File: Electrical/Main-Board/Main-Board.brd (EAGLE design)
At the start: 160 x 100 mm, 10 parts, among them IC1 ATMEGA16A-PU, IC2 ATMEGA16A-PU, J1 FTSH-105-01-L-DV-K-A-P-TR

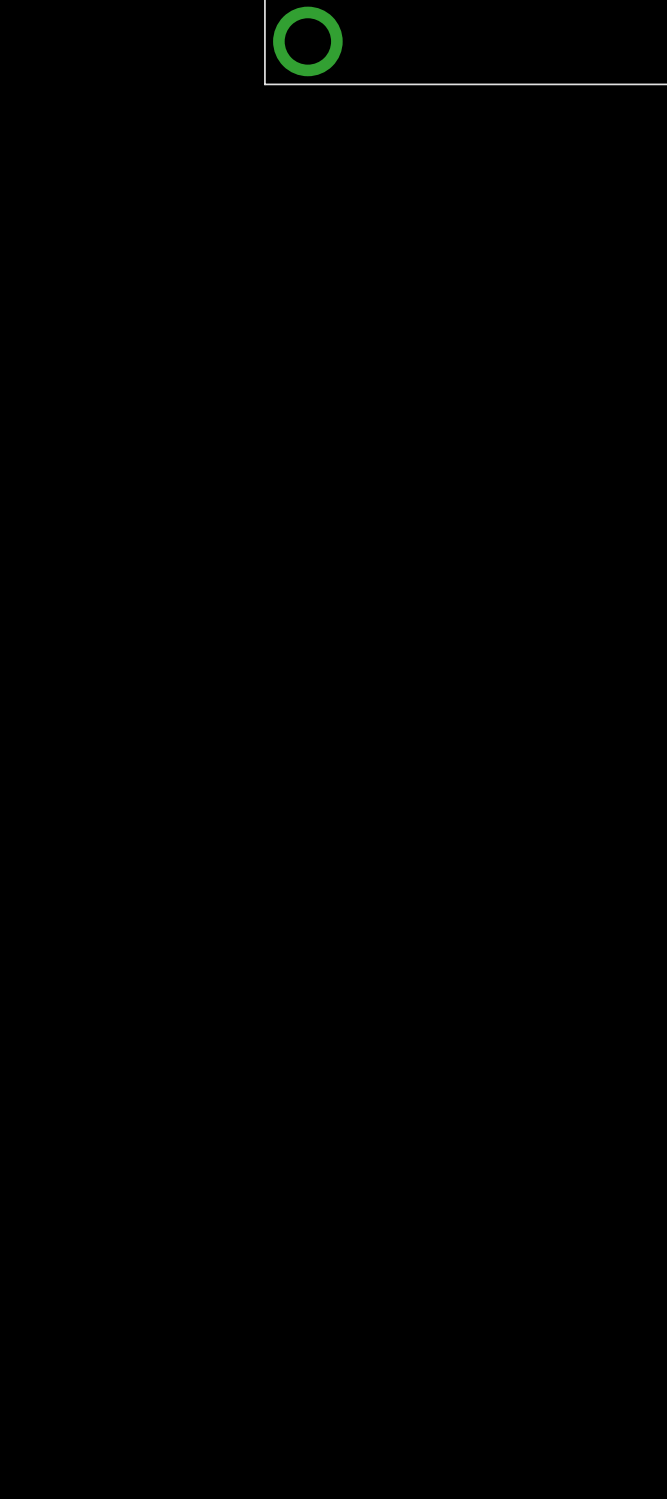
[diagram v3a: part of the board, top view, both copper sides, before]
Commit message: Added motor things to schematic
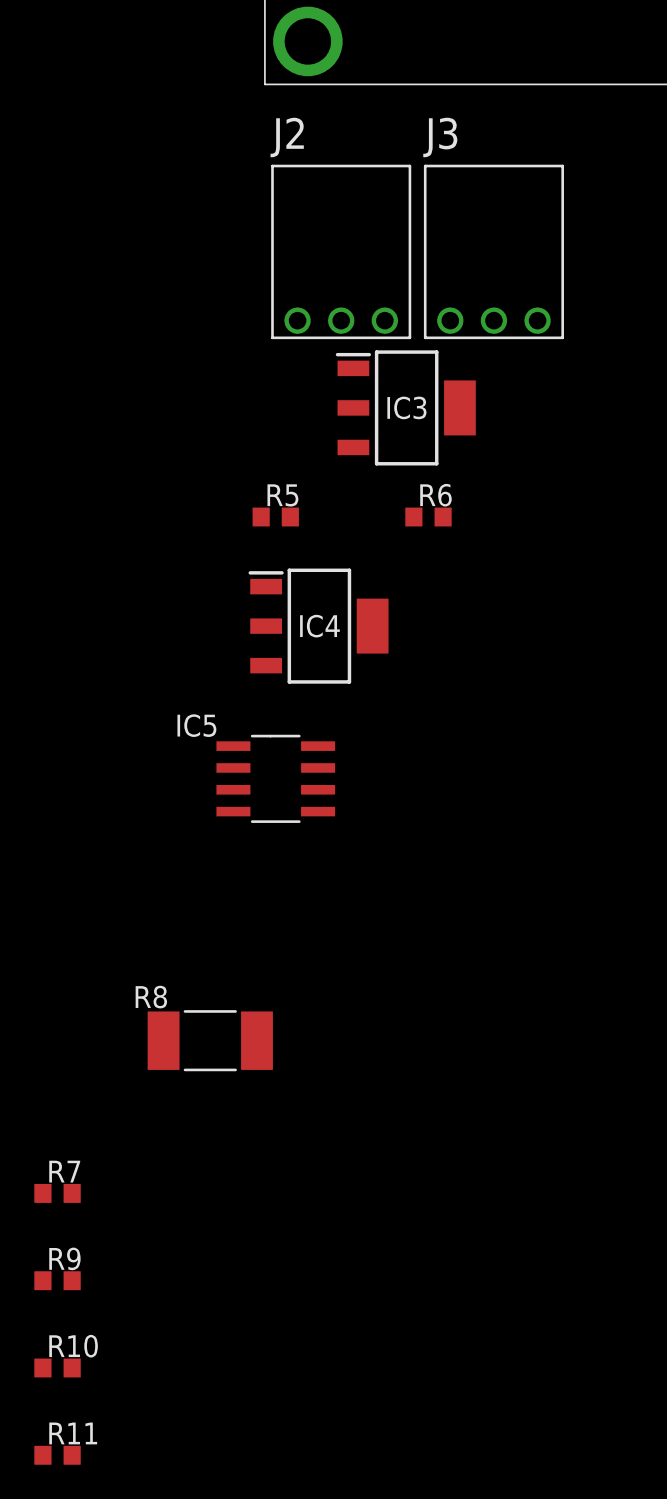
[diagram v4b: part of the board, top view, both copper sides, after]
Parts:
- added IC3: AZ1117CH-ADJTRG1, SamacSys_Parts:SOT230P700X170-4N
- added IC4: AZ1117CH-5.0TRG1DITR-ND, SamacSys_Parts:SOT230P700X180-4N
- added IC5: LM2904DRG3, SamacSys_Parts:SOIC127P600X175-8N
- added J2, J3: 0022288033, 0022288033:0022288033
- added R10, R11: 10K/5%, rcl:R0603
- added R5: 200R/5%, rcl:R0603
- added R6: 866R/5%, rcl:R0603
- added R7, R9: 100R/5%, rcl:R0603
- added R8: ERJ-L1WKF10CU, SamacSys_Parts:RESC6332X120N
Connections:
- new net +12V: IC3.3, IC4.3
- new net +7.5V: J2.P$2, J3.P$2, R8.2, R9.1
- new net DABDA: IC3.2, IC3.4, R5.2, R7.1, R8.1
- new net MOTOR_OVER-CURRENT: IC2.3, IC5.1, R10.2
- new net N$1: IC5.3, R11.2, R7.2
- new net N$5: IC5.2, R10.1, R9.2
- new net SERVO-LOWER: IC2.19, J3.P$3
- new net SERVO-UPPER: IC2.18, J2.P$3
- new net W3R355: IC3.1, R5.1, R6.2
- net +5V/1: now also IC4.2, IC4.4, IC5.8
- net GND: now also IC4.1, IC5.4, J2.P$1, J3.P$1, R11.1, R6.1

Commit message: Did some layout
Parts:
- added J4: PJ-031DH, SamacSys_Parts:PJ031DH
- moved IC5 195.2 mm to (91.0, -16.0)
- moved R7 195.1 mm to (78.0, -40.0)
- moved R6 195.1 mm to (100.0, -1.00)
- moved R5 195.0 mm to (91.0, -1.00)
- moved R11 194.5 mm to (78.0, -56.0)
- moved R10 194.5 mm to (78.0, -51.0)
- moved R9 194.4 mm to (78.0, -46.0)
- moved R8 174.7 mm to (3.00, -8.00)
- moved IC4 166.5 mm to (0.00, 10.0), turned to 90 degrees
- moved DS1 143.9 mm to (0.00, 41.0)
- moved IC3 143.3 mm to (0.00, 0.00), turned to 90 degrees
- moved R4 131.2 mm to (77.0, 12.0)
- moved J3 123.0 mm to (38.0, -30.0), turned to 180 degrees
- moved J2 114.1 mm to (9.90, -30.0), turned to 180 degrees
- moved S2 100.8 mm to (38.0, -6.00), turned to 270 degrees
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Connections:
- net +12V: now also J4.1
- net GND: now also J4.2
- net LCD-E: now also IC1.3; no longer IC1.18
- net LCD-R/W: now also IC1.2; no longer IC1.19
- net LCD-RS: now also IC1.1; no longer IC1.20
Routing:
- net LCD-DB7: track 0.00 -> 82.1 mm, vias 0 -> 1
- net LCD-DB6: track 0.00 -> 62.0 mm
- net LCD-DB5: track 0.00 -> 58.4 mm
- net SDA: track 0.00 -> 57.8 mm
- net SCL: track 0.00 -> 56.5 mm
- net TCK: track 0.00 -> 55.1 mm, vias 0 -> 1
- net LCD-DB4: track 0.00 -> 54.8 mm
- net TMS: track 0.00 -> 54.0 mm, vias 0 -> 1
- net TDI: track 0.00 -> 51.8 mm, vias 0 -> 1
- net LCD-DB3: track 0.00 -> 51.2 mm
- net LCD-E: track 0.00 -> 50.9 mm
- net LCD-DB2: track 0.00 -> 47.6 mm
- net LCD-R/W: track 0.00 -> 47.3 mm
- net LCD-DB1: track 0.00 -> 44.0 mm
- net LCD-RS: track 0.00 -> 43.7 mm
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- added copper zone on layer 16, net +5V
- added copper zone on layer 1, net GND
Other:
- board size 160 x 100 mm -> 84 x 100 mm

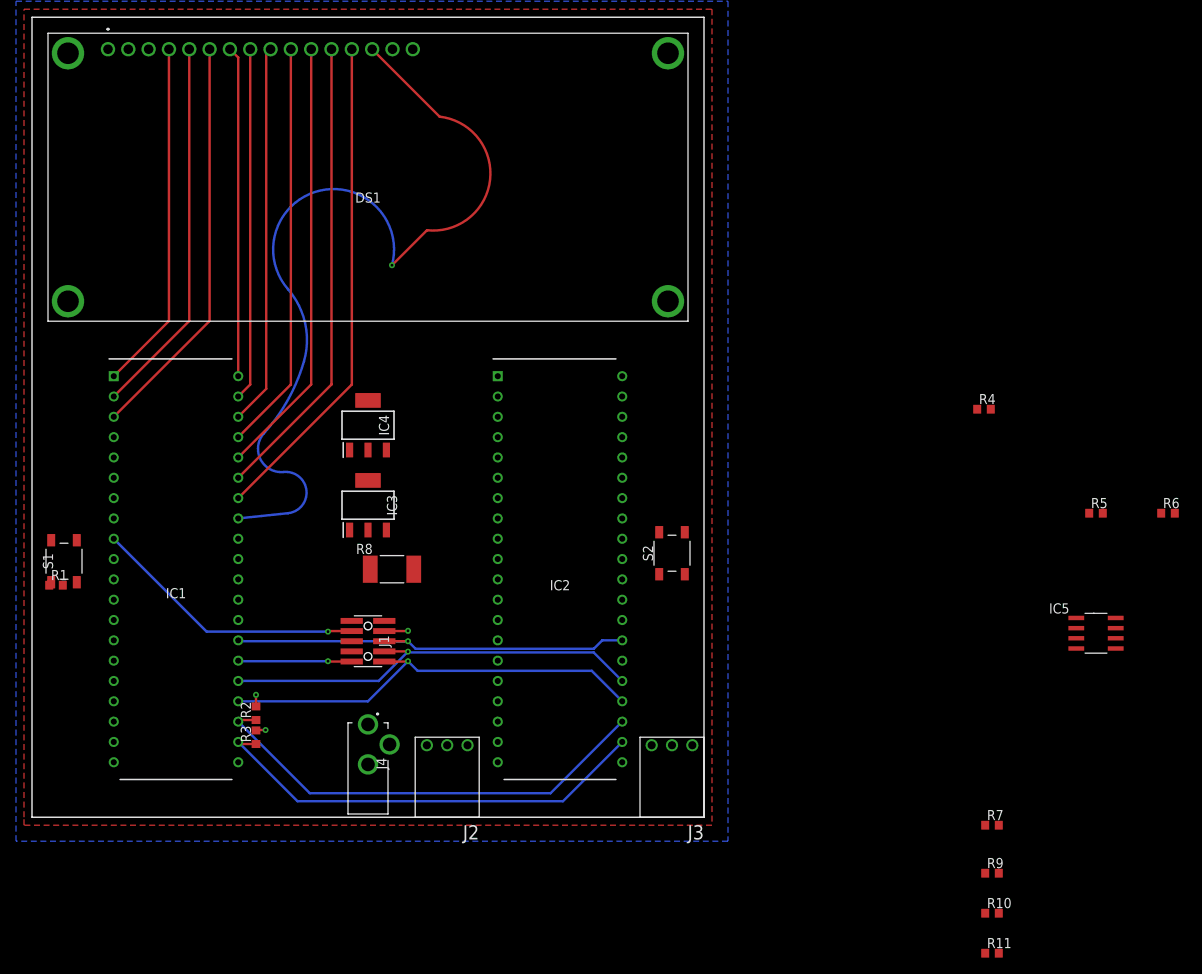
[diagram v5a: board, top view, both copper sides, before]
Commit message: Updated layout
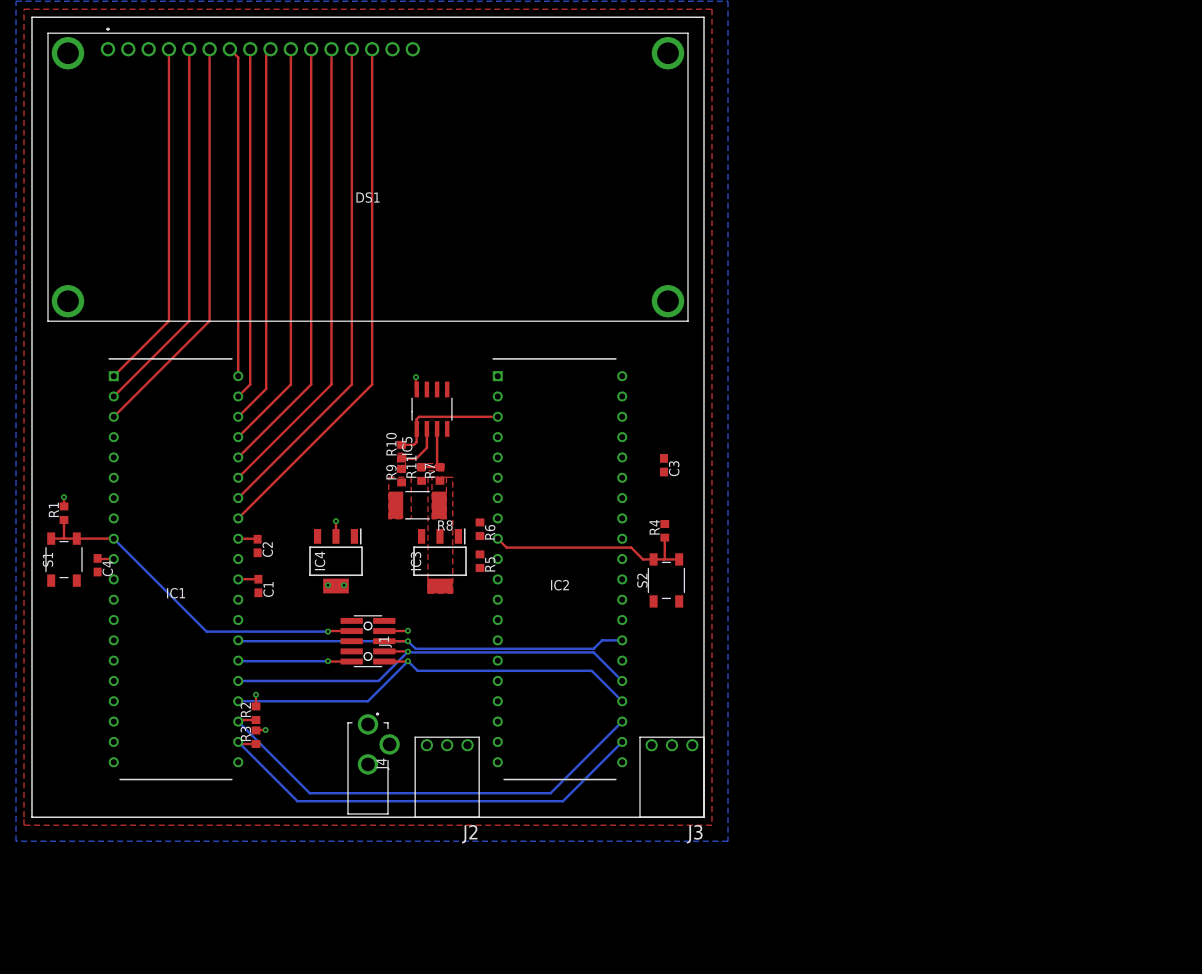
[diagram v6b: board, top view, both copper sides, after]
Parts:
- added C1, C2, C3, C4: 100nF/10%/X7R, rcl:C0603
- moved R10 93.7 mm to (4.20, 6.70), turned to 90 degrees
- moved R11 93.1 mm to (6.70, 3.90), turned to 90 degrees
- moved R9 89.0 mm to (4.20, 3.70), turned to 90 degrees
- moved IC5 87.6 mm to (8.00, 12.0), turned to 90 degrees
- moved R6 86.0 mm to (14.0, -3.00), turned to 270 degrees
- moved R7 81.8 mm to (9.00, 3.90), turned to 90 degrees
- moved R5 77.2 mm to (14.0, -7.00), turned to 270 degrees
- moved R4 42.7 mm to (37.1, -3.20), turned to 90 degrees
- moved IC4 17.5 mm to (-4.00, -7.00), turned to 270 degrees
- moved IC3 11.4 mm to (9.00, -7.00), turned to 270 degrees
- moved R1 9.06 mm to (-38.0, -1.00), turned to 90 degrees
- moved R8 8.62 mm to (6.20, 0.00), turned to 180 degrees
- moved S2 3.47 mm to (37.3, -9.40)
- moved S1 0.20 mm to (-38.0, -6.80)
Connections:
- net +5V/1: now also C1.1, C2.1, C3.1, C4.1
- net GND: now also C1.2, C2.2, C3.2, C4.2
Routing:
- net RST: track 34.6 -> 71.3 mm
- net LCD-DB7: track 82.1 -> 65.6 mm, vias 1 -> 0
- net MOTOR_OVER-CURRENT: track 0.00 -> 15.2 mm
- net +5V/1: track 5.65 -> 17.3 mm, vias 3 -> 8
- net N$1: track 0.00 -> 6.52 mm
- net N$5: track 0.00 -> 6.12 mm
- added copper zone on layer 16, net +5V/1
- added copper zone on layer 1, net +7.5V
- added copper zone on layer 1, net DABDA
- added copper zone on layer 1, net N$1
- added copper zone on layer 1, net N$5
- removed copper zone on layer 16, net +5V

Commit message: Prelimenary layout
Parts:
- moved C3 8.44 mm to (35.0, -3.20), turned to 90 degrees
- moved IC4 3.00 mm to (-1.00, -7.00)
- moved R5 0.30 mm to (13.7, -7.00)
- moved R6 0.30 mm to (13.7, -3.00)
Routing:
- net TDO: track 14.2 -> 52.5 mm, vias 1 -> 2
- net RST: track 71.3 -> 97.7 mm
- net SERVO-LOWER: track 0.00 -> 20.2 mm
- net SERVO-UPPER: track 0.00 -> 10.1 mm
- net +5V/1: track 17.3 -> 24.4 mm
- net DABDA: track 0.00 -> 6.39 mm
- net W3R355: track 0.00 -> 4.72 mm
- added copper zone on layer 1, net +12V
- added copper zone on layer 1, net +5V/1

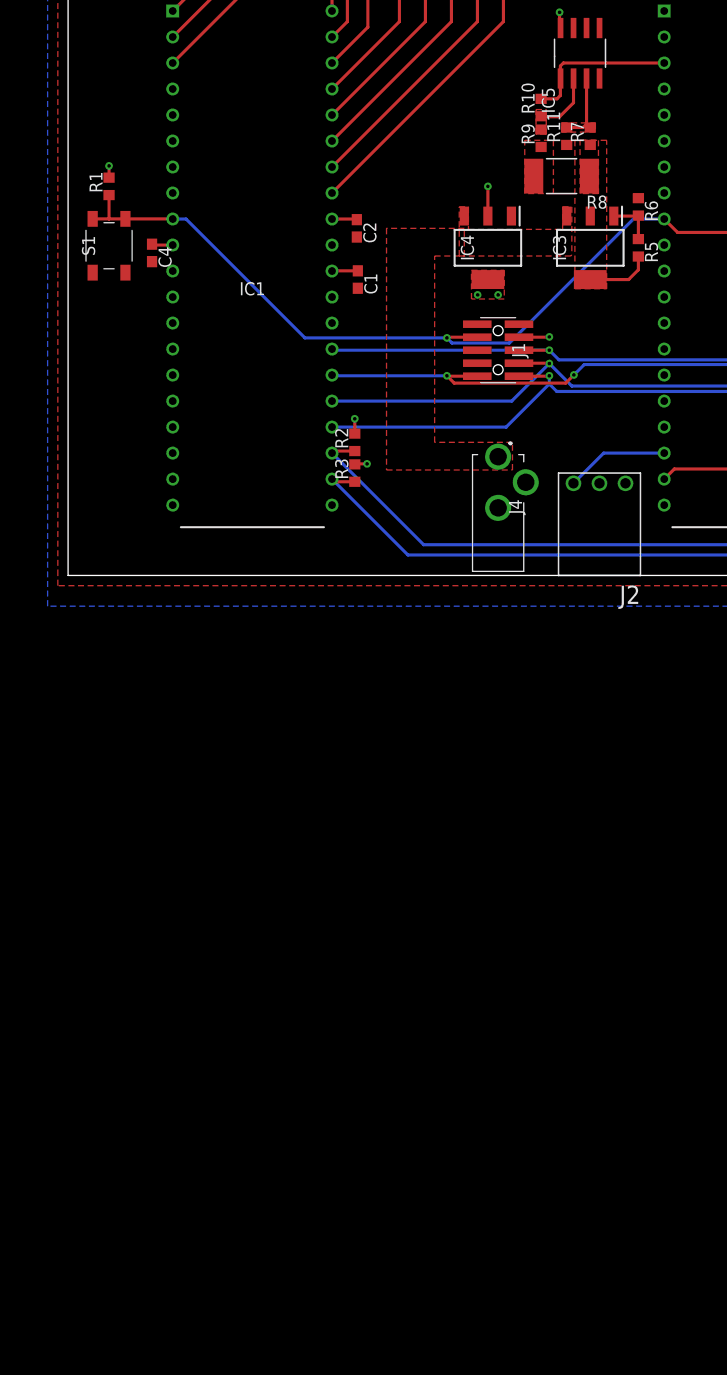
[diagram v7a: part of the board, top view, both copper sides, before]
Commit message: Updated schematci for more componenets
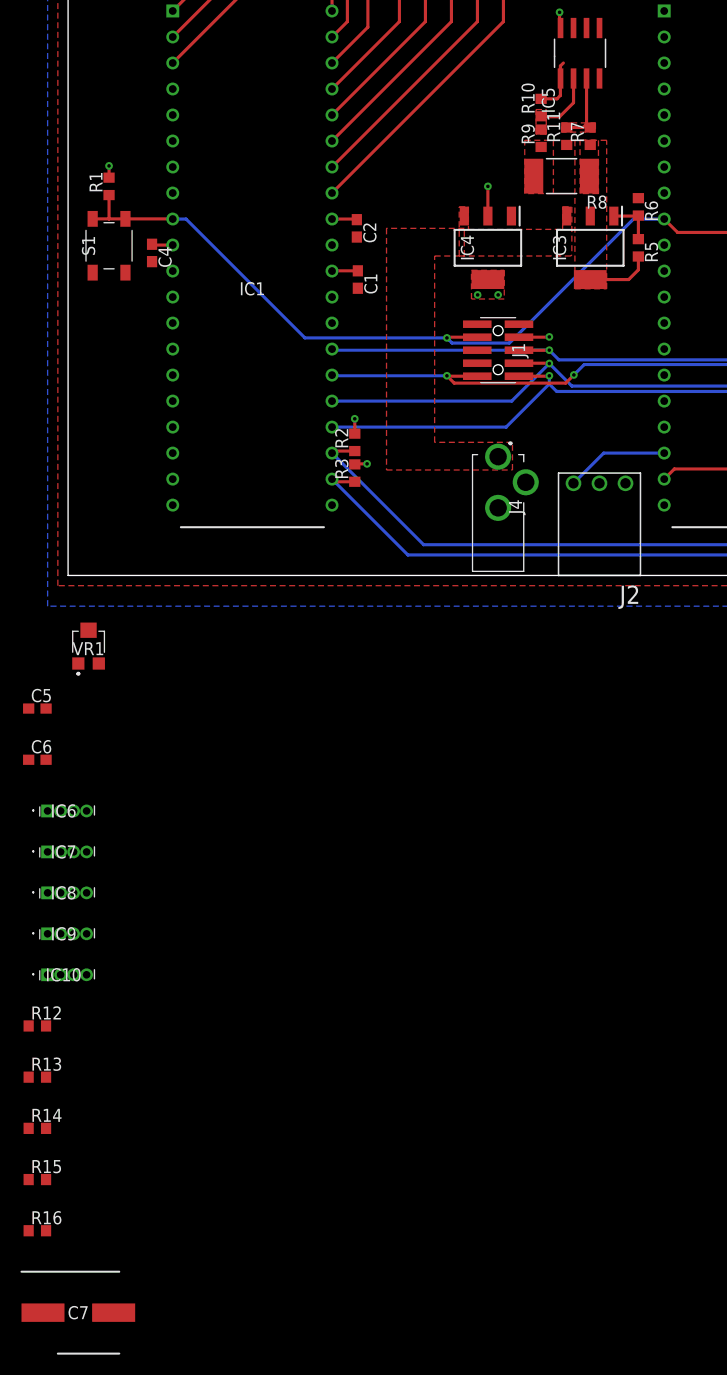
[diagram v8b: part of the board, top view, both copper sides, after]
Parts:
- added C5, C6: 100nF/10%/X7R, rcl:C0603
- added C7: EEEFK1J220P, SamacSys_Parts:CAPAE800X650N
- added IC10, IC6, IC7, IC8, IC9: TLE4966L, SamacSys_Parts:TLE4966L
- added R12, R13, R14, R15, R16: 1.2K/5%, rcl:R0603
- added VR1: EVM3YSX50B54, SamacSys_Parts:EVM3YSX50B54
- R7, R9: value 100R/5% -> 500R/5%
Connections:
- net +12V: now also C7.1
- net +5V/1: now also C5.1, C6.1, VR1.1
- net GND: now also C5.2, C6.2, C7.2, VR1.3
- net MOTOR_OVER-CURRENT: now also IC2.40; no longer IC2.3
- net N$2: now also VR1.2
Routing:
- net MOTOR_OVER-CURRENT: track 15.2 -> 5.33 mm
